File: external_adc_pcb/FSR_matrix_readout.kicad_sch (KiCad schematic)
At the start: 6 parts

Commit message: renmaing and cleanup
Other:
- sheet 16:1_decoder renamed 16:1 Decoder
- sheet adc renamed ADC
- sheet addr_counter renamed Addr Counter
- sheet backend_mux renamed Backend Mux
- sheet dynamic_gain_opamp renamed Programmable Gain Op-amp
- sheet freenove_esp32s3_dev renamed Feenove Esp32s3 Dev Board
- sheet frontend_mux renamed Frontend Analog Switch
- sheet power renamed Power
- sheet sense_opamps renamed TIA Op-amps
- sheet Feenove Esp32s3 Dev Board: file freenove_esp32s3_dev.kicad_sch -> freenove_esp32s3_dev_board.kicad_sch
- sheet Frontend Analog Switch: file frontend_mux.kicad_sch -> frontend_analog_switch.kicad_sch
- sheet Programmable Gain Op-amp: file dynamic_gain_opamp.kicad_sch -> programmable_gain_opamp.kicad_sch
- sheet TIA Op-amps: file sense_opamps.kicad_sch -> tia_opamps.kicad_sch
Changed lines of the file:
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@@
 			(color 0 0 0 0)
 		)
-		(property "Sheetname" "frontend_mux"
+		(property "Sheetname" "Frontend Analog Switch"
 			(at 106.68 53.8984 0)
 			(show_name no)
@@
 			)
 		)
-		(property "Sheetfile" "frontend_mux.kicad_sch"
+		(property "Sheetfile" "frontend_analog_switch.kicad_sch"
 			(at 106.68 50.292 0)
 			(hide yes)
@@
 			(color 0 0 0 0)
 		)
-		(property "Sheetname" "backend_mux"
-			(at 149.225 130.81 0)
+		(property "Sheetname" "Backend Mux"
+			(at 148.59 130.81 0)
 			(show_name no)
 			(do_not_autoplace no)
@@
 			(color 0 0 0 0)
 		)
-		(property "Sheetname" "16:1_decoder"
+		(property "Sheetname" "16:1 Decoder"
 			(at 148.59 55.1684 0)
 			(show_name no)
@@
 			(color 0 0 0 0)
 		)
-		(property "Sheetname" "freenove_esp32s3_dev"
+		(property "Sheetname" "Feenove Esp32s3 Dev Board"
 			(at 176.53 72.9484 0)
 			(show_name no)
@@
 			)
 		)
-		(property "Sheetfile" "freenove_esp32s3_dev.kicad_sch"
+		(property "Sheetfile" "freenove_esp32s3_dev_board.kicad_sch"
 			(at 176.53 89.4846 0)
 			(hide yes)
@@
 			(color 0 0 0 0)
 		)
-		(property "Sheetname" "addr_counter"
+		(property "Sheetname" "Addr Counter"
 			(at 152.4 72.39 0)
 			(show_name no)
@@
 			(color 0 0 0 0)
 		)
-		(property "Sheetname" "power"
+		(property "Sheetname" "Power"
 			(at 107.95 95.8084 0)
 			(show_name no)
@@
 			(color 0 0 0 0)
 		)
-		(property "Sheetname" "adc"
+		(property "Sheetname" "ADC"
 			(at 216.535 123.19 0)
 			(show_name no)
@@
 		(on_board yes)
 		(dnp no)
-		(fields_autoplaced yes)
-		(stroke
-			(width 0.1524)
-			(type solid)
-		)
-		(fill
-			(color 0 0 0 0)
-		)
-		(property "Sheetname" "sense_opamps"
-			(at 106.68 119.9384 0)
-			(show_name no)
-			(do_not_autoplace no)
-			(effects
-				(font
-					(size 1.27 1.27)
-				)
-				(justify left bottom)
-			)
-		)
-		(property "Sheetfile" "sense_opamps.kicad_sch"
+		(stroke
+			(width 0.1524)
+			(type solid)
+		)
+		(fill
+			(color 0 0 0 0)
+		)
+		(property "Sheetname" "TIA Op-amps"
+			(at 106.68 130.81 0)
+			(show_name no)
+			(do_not_autoplace no)
+			(effects
+				(font
+					(size 1.27 1.27)
+				)
+				(justify left bottom)
+			)
+		)
+		(property "Sheetfile" "tia_opamps.kicad_sch"
 			(at 106.68 128.8546 0)
 			(hide yes)
@@
 			(color 0 0 0 0)
 		)
-		(property "Sheetname" "dynamic_gain_opamp"
+		(property "Sheetname" "Programmable Gain Op-amp"
 			(at 176.53 127 0)
 			(show_name no)
@@
 			)
 		)
-		(property "Sheetfile" "dynamic_gain_opamp.kicad_sch"
+		(property "Sheetfile" "programmable_gain_opamp.kicad_sch"
 			(at 176.53 125.0446 0)
 			(hide yes)

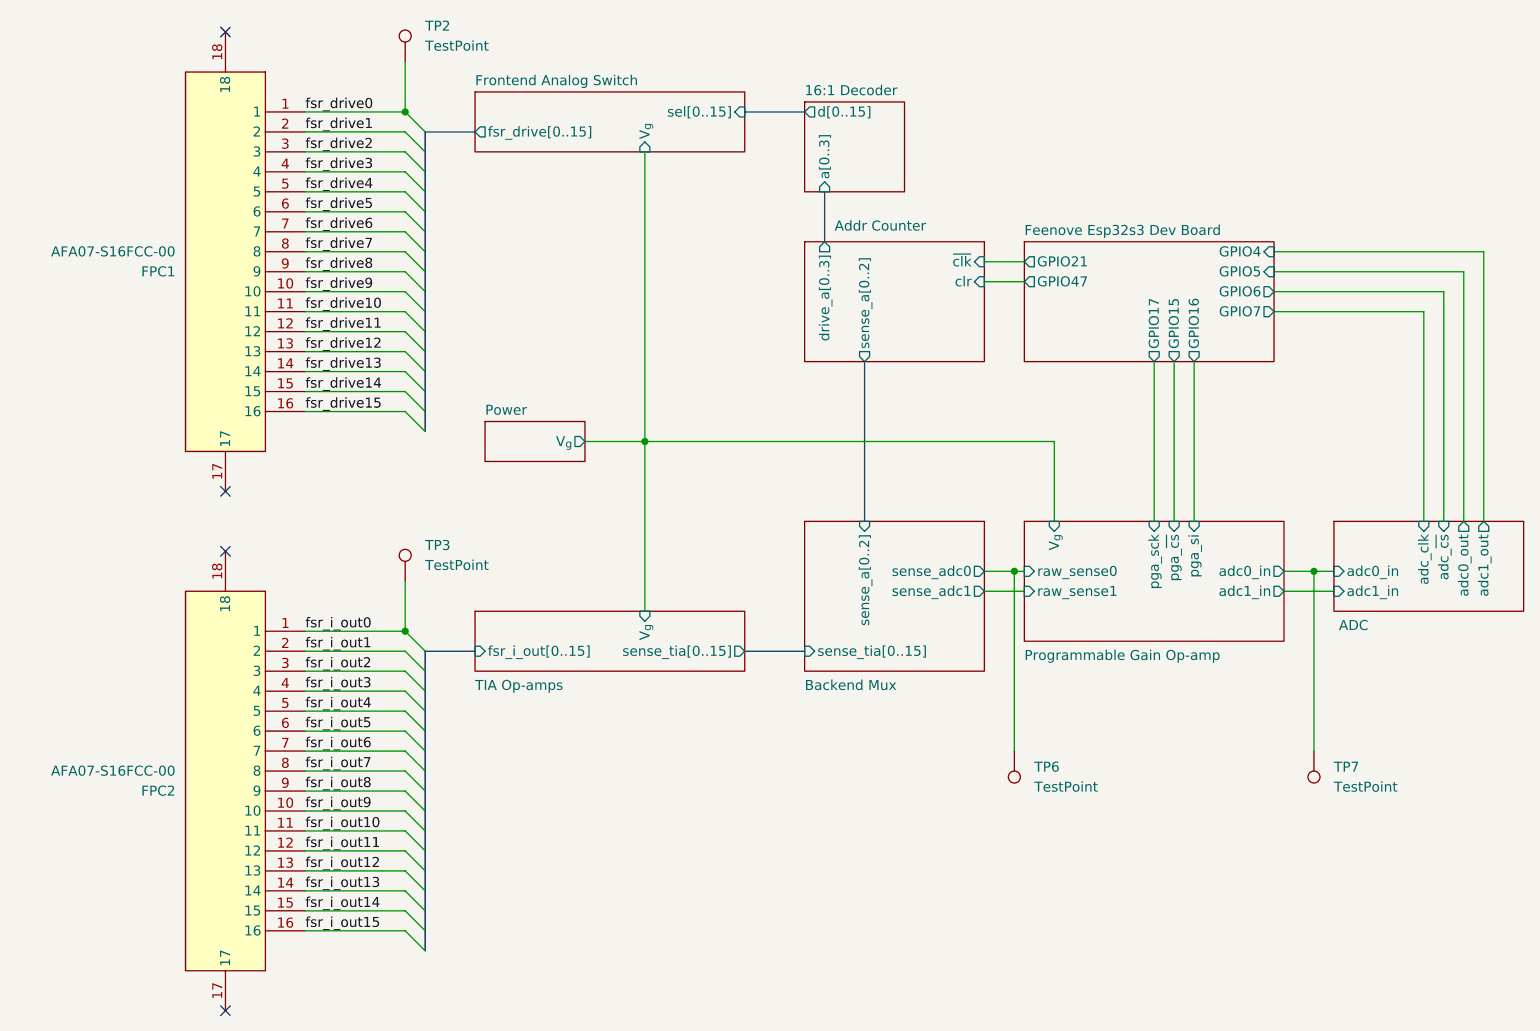
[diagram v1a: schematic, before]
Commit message: capitalize netnames; change and embed font
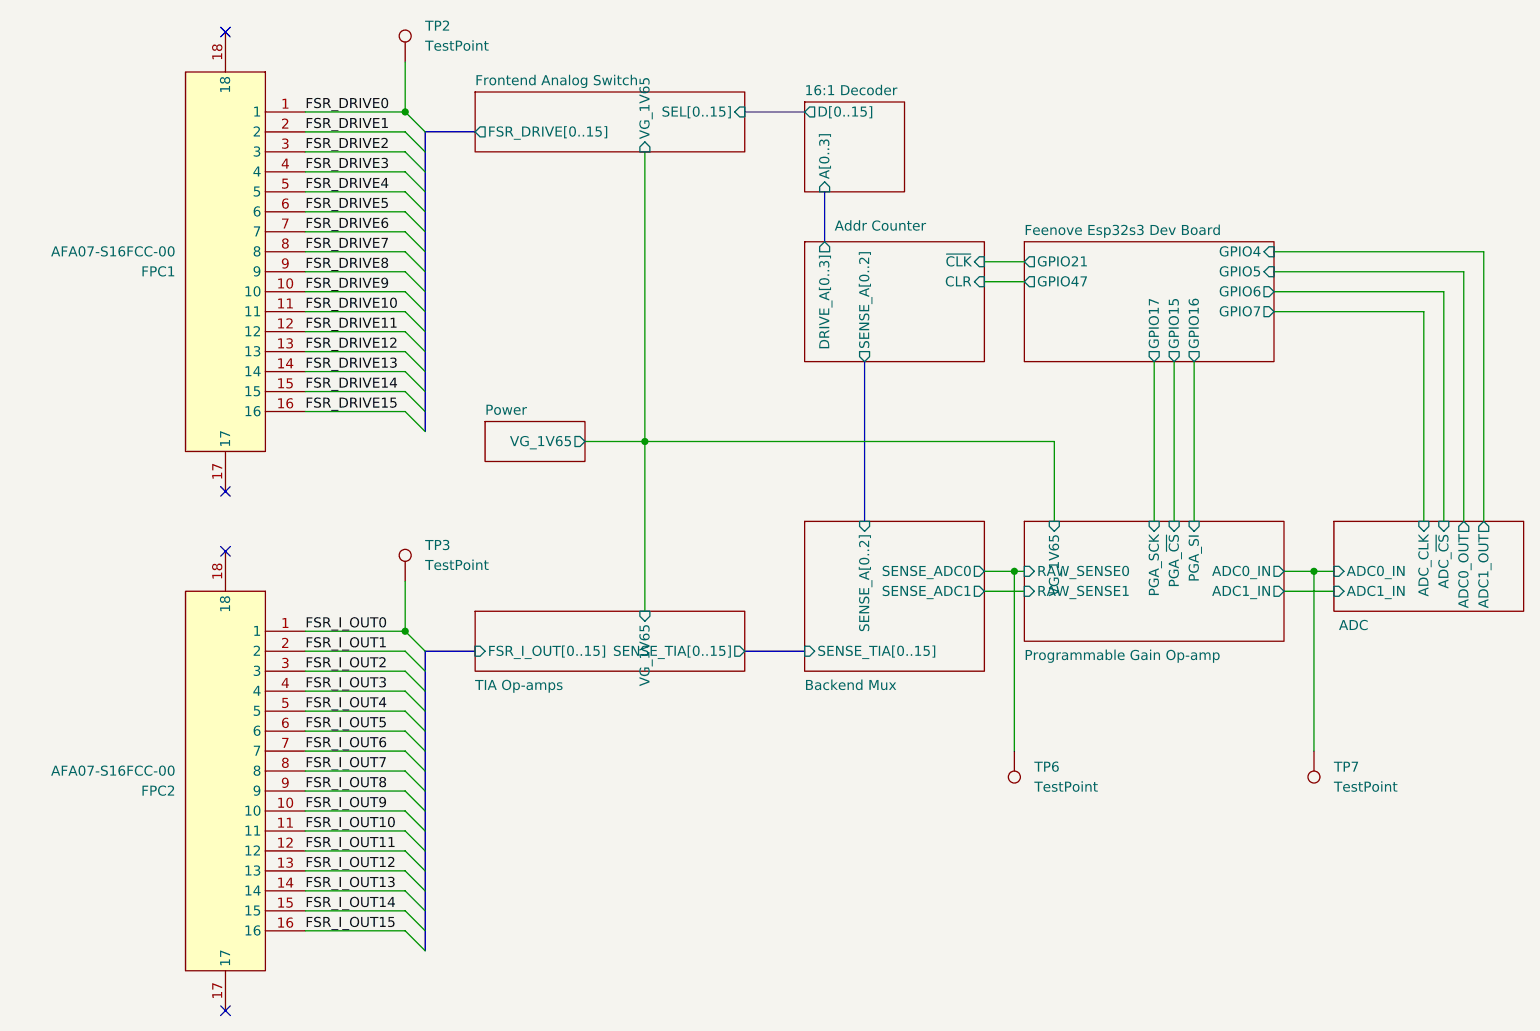
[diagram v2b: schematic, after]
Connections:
- net ADC/adc0_in renamed ADC/ADC0_IN
- net Backend Mux/sense_adc0 renamed Backend Mux/SENSE_ADC0
- net fsr_drive0 renamed FSR_DRIVE0
- net fsr_drive1 renamed FSR_DRIVE1
- net fsr_drive10 renamed FSR_DRIVE10
- net fsr_drive11 renamed FSR_DRIVE11
- net fsr_drive12 renamed FSR_DRIVE12
- net fsr_drive13 renamed FSR_DRIVE13
- net fsr_drive14 renamed FSR_DRIVE14
- net fsr_drive15 renamed FSR_DRIVE15
- net fsr_drive2 renamed FSR_DRIVE2
- net fsr_drive3 renamed FSR_DRIVE3
- net fsr_drive4 renamed FSR_DRIVE4
- net fsr_drive5 renamed FSR_DRIVE5
- net fsr_drive6 renamed FSR_DRIVE6
- net fsr_drive7 renamed FSR_DRIVE7
- net fsr_drive8 renamed FSR_DRIVE8
- net fsr_drive9 renamed FSR_DRIVE9
- net fsr_i_out0 renamed FSR_I_OUT0
- net fsr_i_out1 renamed FSR_I_OUT1
- net fsr_i_out10 renamed FSR_I_OUT10
- net fsr_i_out11 renamed FSR_I_OUT11
- net fsr_i_out12 renamed FSR_I_OUT12
- net fsr_i_out13 renamed FSR_I_OUT13
- net fsr_i_out14 renamed FSR_I_OUT14
- net fsr_i_out15 renamed FSR_I_OUT15
- net fsr_i_out2 renamed FSR_I_OUT2
- net fsr_i_out3 renamed FSR_I_OUT3
- net fsr_i_out4 renamed FSR_I_OUT4
- net fsr_i_out5 renamed FSR_I_OUT5
- net fsr_i_out6 renamed FSR_I_OUT6
- net fsr_i_out7 renamed FSR_I_OUT7
- net fsr_i_out8 renamed FSR_I_OUT8
- net fsr_i_out9 renamed FSR_I_OUT9
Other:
- sheet 16:1 Decoder ports: added A[0..3], D[0..15]; removed a[0..3], d[0..15]
- sheet ADC ports: added ADC0_IN, ADC0_OUT, ADC1_IN, ADC1_OUT, ADC_CLK, ADC_~{CS}; removed adc0_in, adc0_out, adc1_in, adc1_out, adc_clk, adc_~{cs}
- sheet Addr Counter ports: added CLR, DRIVE_A[0..3], SENSE_A[0..2], ~{CLK}; removed clr, drive_a[0..3], sense_a[0..2], ~{clk}
- sheet Backend Mux ports: added SENSE_ADC0, SENSE_ADC1, SENSE_A[0..2], SENSE_TIA[0..15]; removed sense_a[0..2], sense_adc0, sense_adc1, sense_tia[0..15]
- sheet Frontend Analog Switch ports: added FSR_DRIVE[0..15], SEL[0..15], VG_1V65; removed V_{g}, fsr_drive[0..15], sel[0..15]
- sheet Power ports: added VG_1V65; removed V_{g}
- sheet Programmable Gain Op-amp ports: added ADC0_IN, ADC1_IN, PGA_SCK, PGA_SI, PGA_~{CS}, RAW_SENSE0, RAW_SENSE1, VG_1V65; removed V_{g}, adc0_in, adc1_in, pga_sck, pga_si, pga_~{cs}, raw_sense0, raw_sense1
- sheet TIA Op-amps ports: added FSR_I_OUT[0..15], SENSE_TIA[0..15], VG_1V65; removed V_{g}, fsr_i_out[0..15], sense_tia[0..15]
